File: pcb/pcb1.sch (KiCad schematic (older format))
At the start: 11 parts, among them J1 Screw_Terminal_01x02, J2 Screw_Terminal_01x02, K1 JQC-3F-_T73_-1Z-12VDC, K2 JQC-3F-_T73_-1Z-12VDC, Q1 BC547, Q2 BC547

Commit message: On attiny85 with UART Serial Support - New firmware included
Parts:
- removed A1: Arduino_Nano_v3.x, Module:Arduino_Nano, symbol MCU_Module:Arduino_Nano_v3.x
- added C1, C2: 22pF, Capacitor_THT:C_Disc_D5.0mm_W2.5mm_P5.00mm, symbol Device:C_Small
- added C3: 0.1uF, Capacitor_THT:CP_Radial_D5.0mm_P2.00mm, symbol Device:CP1
- added J3: USB_A, Connector_USB:USB_A_Molex_105057_Vertical, symbol Connector:USB_A
- added J4, J5: Conn_01x08_Male, Connector_PinHeader_2.54mm:PinHeader_1x08_P2.54mm_Horizontal, symbol Connector:Conn_01x08_Male
- added U1: ATtiny85-20PU, Package_DIP:DIP-8_W7.62mm, symbol MCU_Microchip_ATtiny:ATtiny85-20PU
- added Y1: Crystal, Crystal:Crystal_HC49-4H_Vertical, symbol Device:Crystal
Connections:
- wire segments 44 -> 95
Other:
- moved on the sheet: D1, D2, J1, J2, K1, K2, Q1, Q2, R1, R2

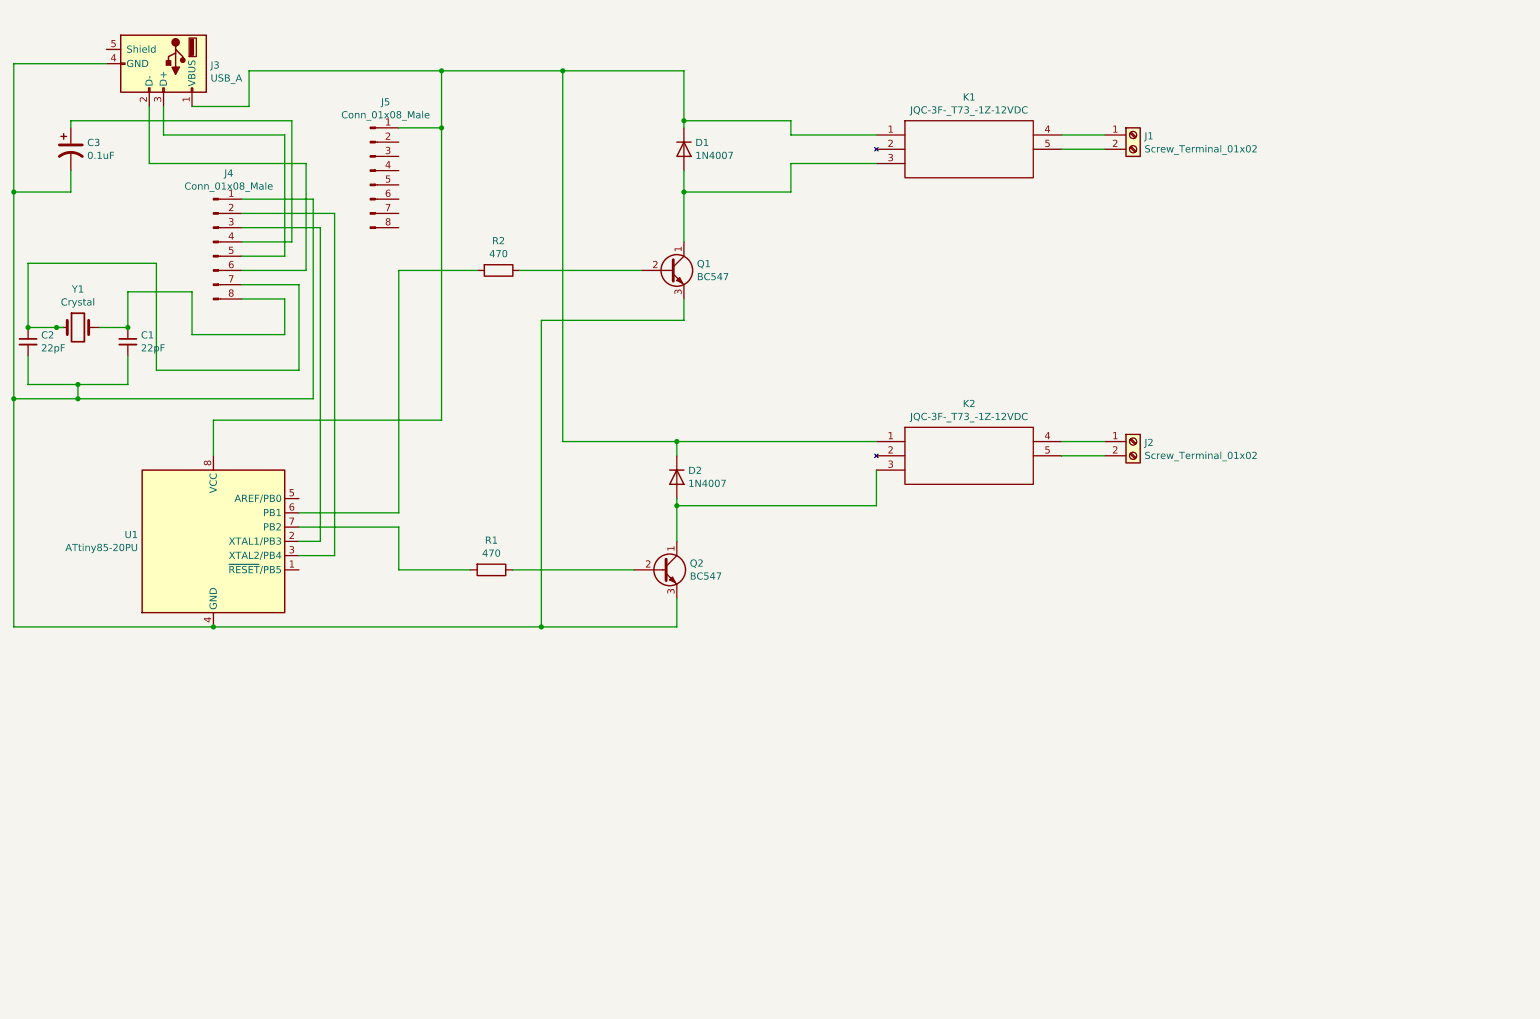
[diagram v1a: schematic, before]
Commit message: attiny85, 4 relay edition - Added MUX for greater pin support
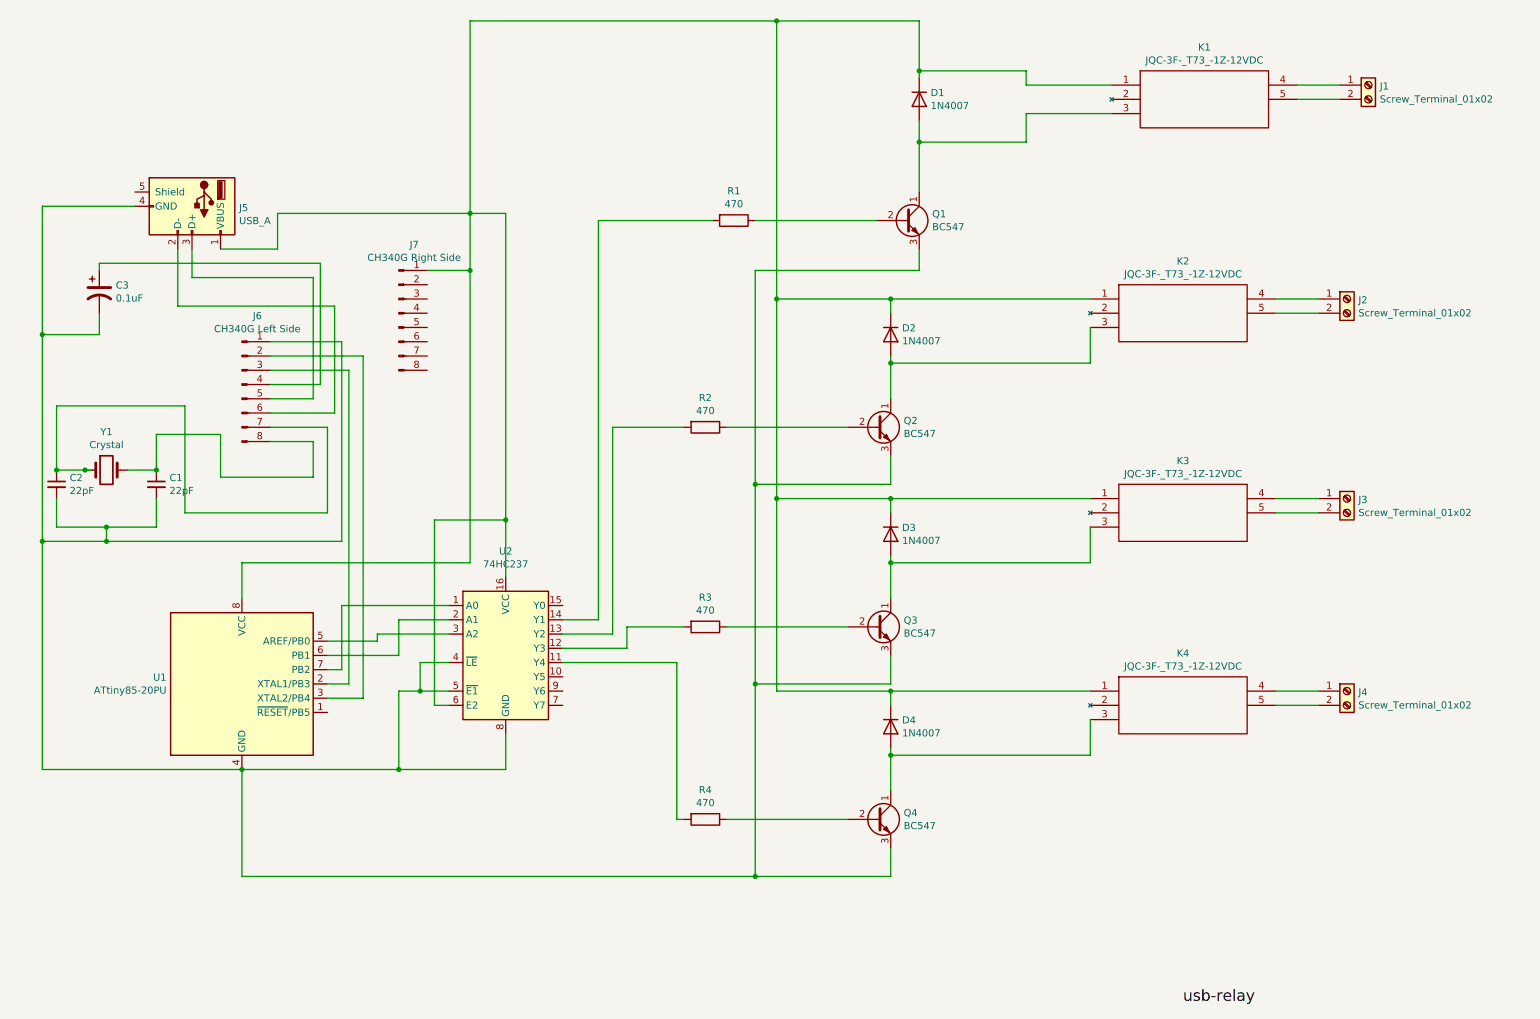
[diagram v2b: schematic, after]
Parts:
- added D3, D4: 1N4007, Diode_THT:D_DO-41_SOD81_P10.16mm_Horizontal, symbol Diode:1N4007
- added J3, J4: Screw_Terminal_01x02, TerminalBlock:TerminalBlock_Altech_AK300-2_P5.00mm, symbol Connector:Screw_Terminal_01x02
- added K3, K4: JQC-3F-_T73_-1Z-12VDC, JQC-3F-_T73_-1Z-12VDC:JQC3FT731Z12VDC, symbol JQC-3F-_T73_-1Z-12VDC:JQC-3F-_T73_-1Z-12VDC
- added Q3, Q4: BC547, Package_TO_SOT_THT:TO-92_Inline, symbol Transistor_BJT:BC547
- added R3, R4: 470, Resistor_THT:R_Axial_DIN0411_L9.9mm_D3.6mm_P12.70mm_Horizontal, symbol Device:R
- added U2: 74HC237, Package_DIP:DIP-16_W7.62mm, symbol 74xx:74HC237
- J6: renamed from J4; value Conn_01x08_Male -> CH340G Left Side
- J7: renamed from J5; value Conn_01x08_Male -> CH340G Right Side
- renumbered J3 to J5, R2 to R1, R1 to R2
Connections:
- net at C1.2, C2.2, C3.2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: now also Q3.3 (E), Q4.3 (E), U2.4 (~LE), U2.5 (~E1), U2.8 (GND)
- net at D1.1 (K), D2.1 (K), J5.1 (VBUS)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: now also D3.1 (K), D4.1 (K), K3.1, K4.1, U2.16 (VCC), U2.6 (E2)
- net at R2.2: now also U2.13 (Y2); no longer U1.7 (PB2)
- net at R1.2: now also U2.14 (Y1); no longer U1.6 (PB1)
- net at U1.5 (AREF/PB0): now also U2.3 (A2)
- new net: U1.6 (PB1), U2.2 (A1)
- new net: U1.7 (PB2), U2.1 (A0)
- new net: R4.2, U2.11 (Y4)
- new net: R3.2, U2.12 (Y3)
- new net: D3.2 (A), K3.3, Q3.1 (C)
- new net: Q3.2 (B), R3.1
- new net: J3.1 (Pin_1), K3.4
- new net: J3.2 (Pin_2), K3.5
- new net: D4.2 (A), K4.3, Q4.1 (C)
- new net: Q4.2 (B), R4.1
- new net: J4.1 (Pin_1), K4.4
- new net: J4.2 (Pin_2), K4.5
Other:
- moved on the sheet: C1, C2, C3, D1, D2, J1, J2, J5, J6, J7, K1, K2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

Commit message: atmega328p - THT version
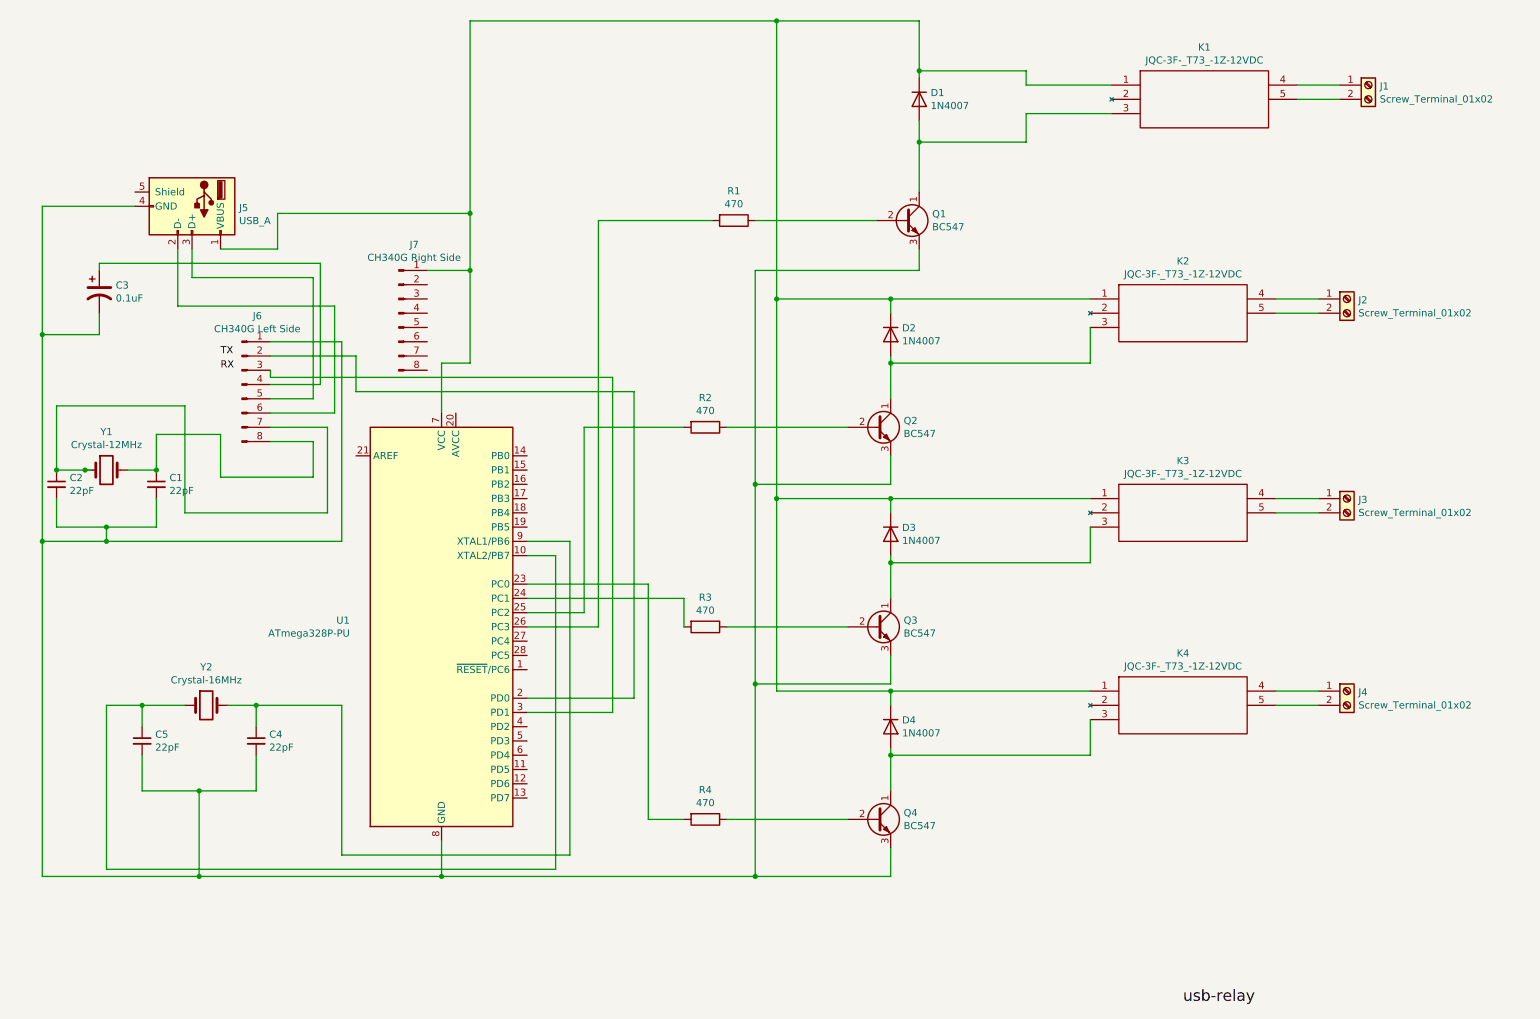
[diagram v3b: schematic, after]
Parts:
- removed U1: ATtiny85-20PU, Package_DIP:DIP-8_W7.62mm, symbol MCU_Microchip_ATtiny:ATtiny85-20PU
- removed U2: 74HC237, Package_DIP:DIP-16_W7.62mm, symbol 74xx:74HC237
- added C4, C5: 22pF, Capacitor_THT:C_Disc_D5.0mm_W2.5mm_P5.00mm, symbol Device:C_Small
- added U1: ATmega328P-PU, Package_DIP:DIP-28_W7.62mm, symbol MCU_Microchip_ATmega:ATmega328P-PU
- added Y2: Crystal-16MHz, Crystal:Crystal_HC49-4H_Vertical, symbol Device:Crystal
- Y1: value Crystal -> Crystal-12MHz
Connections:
- net at C1.2, C2.2, C3.2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: now also C4.2, C5.2, U1.22 (GND), U1.8 (GND)
- net at D1.1 (K), D2.1 (K), D3.1 (K)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: now also U1.7 (VCC)
- net at R2.2: now also U1.25 (PC2)
- net at R1.2: now also U1.26 (PC3)
- net at J6.3 (Pin_3): now also U1.3 (PD1)
- net at J6.2 (Pin_2): now also U1.2 (PD0)
- net at R4.2: now also U1.23 (PC0)
- net at R3.2: now also U1.24 (PC1)
- new net: C5.1, U1.10 (XTAL2/PB7), Y2.1
- new net: C4.1, U1.9 (XTAL1/PB6), Y2.2
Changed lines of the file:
@@
 $EndDescr
-$Comp
-L MCU_Microchip_ATtiny:ATtiny85-20PU U1
-U 1 1 6058B098
-P 2150 5250
-F 0 "U1" H 1621 5296 50  0000 R CNN
-F 1 "ATtiny85-20PU" H 1621 5205 50  0000 R CNN
-F 2 "Package_DIP:DIP-8_W7.62mm" H 2150 5250 50  0001 C CIN
-F 3 "http://ww1.microchip.com/downloads/en/DeviceDoc/atmel-2586-avr-8-bit-microcontroller-attiny25-attiny45-attiny85_datasheet.pdf" H 2150 5250 50  0001 C CNN
-	1    2150 5250
-	1    0    0    -1
-$EndComp
 $Comp
 L Transistor_BJT:BC547 Q2
@@
 P 1200 3750
 F 0 "Y1" H 1200 4018 50  0000 C CNN
-F 1 "Crystal" H 1200 3927 50  0000 C CNN
+F 1 "Crystal-12MHz" H 1200 3927 50  0000 C CNN
 F 2 "Crystal:Crystal_HC49-4H_Vertical" H 1200 3750 50  0001 C CNN
 F 3 "~" H 1200 3750 50  0001 C CNN
@@
 	1200 4150 850  4150
 Wire Wire Line
-	1400 1900 750  1900
-Wire Wire Line
 	750  1900 750  2800
 Wire Wire Line
@@
 Wire Wire Line
 	1050 3750 850  3750
-Wire Wire Line
-	2150 5850 750  5850
-Wire Wire Line
-	750  5850 750  4250
 Connection ~ 750  4250
 $Comp
@@
 	2000 2200 2400 2200
 Wire Wire Line
-	2150 4650 2150 4400
-Wire Wire Line
 	2400 1950 2400 2200
 Wire Wire Line
@@
 Wire Wire Line
 	6900 2200 6900 2350
-Wire Wire Line
-	2900 5250 2750 5250
-Wire Wire Line
-	2750 5350 3000 5350
 $Comp
 L Connector:Conn_01x08_Male J6
@@
 $EndComp
 Wire Wire Line
-	2150 4400 3750 4400
-Wire Wire Line
-	3750 4400 3750 2350
-Wire Wire Line
 	3750 2350 3450 2350
 Wire Wire Line
 	3750 1950 3750 2350
-Wire Wire Line
-	3750 1950 2400 1950
-Connection ~ 3750 2350
 Wire Wire Line
 	1750 3300 850  3300
@@
 	2350 3150 2700 3150
 Wire Wire Line
-	2900 3050 2350 3050
-Wire Wire Line
-	2900 5250 2900 3050
-Wire Wire Line
-	3000 2950 3000 5350
-Wire Wire Line
-	2350 2950 3000 2950
-Wire Wire Line
-	2850 2850 2850 4250
-Wire Wire Line
 	2350 2850 2850 2850
-$Comp
-L 74xx:74HC237 U2
-U 1 1 605E4E2C
-P 4000 5100
-F 0 "U2" H 4000 5881 50  0000 C CNN
-F 1 "74HC237" H 4000 5790 50  0000 C CNN
-F 2 "Package_DIP:DIP-16_W7.62mm" H 4000 5100 50  0001 C CNN
-F 3 "http://www.ti.com/lit/ds/symlink/cd74hc237.pdf" H 4000 5100 50  0001 C CNN
-	1    4000 5100
-	1    0    0    -1
-$EndComp
-Wire Wire Line
-	2750 5050 3250 5050
-Wire Wire Line
-	3250 5050 3250 4800
-Wire Wire Line
-	3250 4800 3600 4800
 Wire Wire Line
 	5750 3850 5750 2350
@@
 Wire Wire Line
 	6700 5250 5750 5250
-Wire Wire Line
-	5450 2000 4650 2000
-Wire Wire Line
-	4650 2000 4650 4800
-Wire Wire Line
-	4650 4800 4400 4800
-Wire Wire Line
-	4400 4900 4750 4900
-Wire Wire Line
-	4750 4900 4750 3450
-Wire Wire Line
-	4750 3450 5250 3450
-Wire Wire Line
-	5250 4850 4850 4850
-Wire Wire Line
-	4850 4850 4850 5000
-Wire Wire Line
-	4850 5000 4400 5000
 $Comp
 L Transistor_BJT:BC547 Q4
@@
 Connection ~ 6700 5300
 Wire Wire Line
-	4400 5100 5200 5100
-Wire Wire Line
-	5200 5100 5200 6200
-Wire Wire Line
-	5200 6200 5250 6200
-Wire Wire Line
 	6700 6600 5750 6600
-Wire Wire Line
-	2150 6600 2150 5850
-Connection ~ 2150 5850
-Wire Wire Line
-	4000 5600 4000 5850
-Wire Wire Line
-	4000 5850 3250 5850
-Wire Wire Line
-	3600 5300 3400 5300
-Wire Wire Line
-	3250 5300 3250 5850
-Connection ~ 3250 5850
-Wire Wire Line
-	3250 5850 2150 5850
-Wire Wire Line
-	4000 4500 4000 4100
-Wire Wire Line
-	4000 1950 3750 1950
-Wire Wire Line
-	3600 5400 3500 5400
-Wire Wire Line
-	3500 5400 3500 4100
-Wire Wire Line
-	3500 4100 4000 4100
-Connection ~ 4000 4100
-Wire Wire Line
-	4000 4100 4000 1950
-Wire Wire Line
-	3600 5100 3400 5100
-Wire Wire Line
-	3400 5100 3400 5300
-Connection ~ 3400 5300
-Wire Wire Line
-	3400 5300 3250 5300
 Text Label 8750 7500 0    79   ~ 0
 usb-relay
-Wire Wire Line
-	3600 4900 3100 4900
-Wire Wire Line
-	3100 4900 3100 4950
-Wire Wire Line
-	3100 4950 2750 4950
-Wire Wire Line
-	3600 4700 2850 4700
-Wire Wire Line
-	2850 4700 2850 5150
-Wire Wire Line
-	2850 5150 2750 5150
 Wire Wire Line
 	5550 6200 6400 6200
@@
 Connection ~ 5750 6600
 Wire Wire Line
-	5750 6600 2150 6600
+	750  4250 750  6600
+Wire Wire Line
+	750  6600 1850 6600
+Wire Wire Line
+	4900 5350 4900 3200
+Wire Wire Line
+	4900 3200 2950 3200
+Wire Wire Line
+	2950 3200 2950 2950
+Wire Wire Line
+	2950 2950 2350 2950
+Wire Wire Line
+	4750 3100 2350 3100
+Wire Wire Line
+	2350 3100 2350 3050
+Text Label 2000 2950 0    50   ~ 0
+TX
+Text Label 2000 3050 0    50   ~ 0
+RX
+$Comp
+L Device:Crystal Y2
+U 1 1 6069FCFD
+P 1900 5400
+F 0 "Y2" H 1900 5668 50  0000 C CNN
+F 1 "Crystal-16MHz" H 1900 5577 50  0000 C CNN
+F 2 "Crystal:Crystal_HC49-4H_Vertical" H 1900 5400 50  0001 C CNN
+F 3 "~" H 1900 5400 50  0001 C CNN
+	1    1900 5400
+	1    0    0    -1
+$EndComp
+$Comp
+L Device:C_Small C5
+U 1 1 606A3350
+P 1450 5650
+F 0 "C5" H 1542 5696 50  0000 L CNN
+F 1 "22pF" H 1542 5605 50  0000 L CNN
+F 2 "Capacitor_THT:C_Disc_D5.0mm_W2.5mm_P5.00mm" H 1450 5650 50  0001 C CNN
+F 3 "~" H 1450 5650 50  0001 C CNN
+	1    1450 5650
+	1    0    0    -1
+$EndComp
+$Comp
+L Device:C_Small C4
+U 1 1 606A8D1A
+P 2250 5650
+F 0 "C4" H 2342 5696 50  0000 L CNN
+F 1 "22pF" H 2342 5605 50  0000 L CNN
+F 2 "Capacitor_THT:C_Disc_D5.0mm_W2.5mm_P5.00mm" H 2250 5650 50  0001 C CNN
+F 3 "~" H 2250 5650 50  0001 C CNN
+	1    2250 5650
+	1    0    0    -1
+$EndComp
+Wire Wire Line
+	2250 5750 2250 6000
+Wire Wire Line
+	2250 6000 1850 6000
+Wire Wire Line
+	1450 6000 1450 5750
+Wire Wire Line
+	1850 6000 1850 6600
+Connection ~ 1850 6000
+Wire Wire Line
+	1850 6000 1450 6000
+Connection ~ 1850 6600
+Wire Wire Line
+	1850 6600 3550 6600
+Wire Wire Line
+	2050 5400 2250 5400
+Wire Wire Line
+	2250 5400 2250 5550
+Wire Wire Line
+	1750 5400 1450 5400
+Wire Wire Line
+	1450 5400 1450 5550
+Wire Wire Line
+	4750 5450 4750 3100
+Wire Wire Line
+	2850 2850 2850 4250
+$Comp
+L MCU_Microchip_ATmega:ATmega328P-PU U1
+U 1 1 6065D461
+P 3550 4850
+F 0 "U1" H 2906 4896 50  0000 R CNN
+F 1 "ATmega328P-PU" H 2906 4805 50  0000 R CNN
+F 2 "Package_DIP:DIP-28_W7.62mm" H 3550 4850 50  0001 C CIN
+F 3 "http://ww1.microchip.com/downloads/en/DeviceDoc/ATmega328_P%20AVR%20MCU%20with%20picoPower%20Technology%20Data%20Sheet%2040001984A.pdf" H 3550 4850 50  0001 C CNN
+	1    3550 4850
+	1    0    0    -1
+$EndComp
+Wire Wire Line
+	4150 5350 4900 5350
+Wire Wire Line
+	4150 5450 4750 5450
+Wire Wire Line
+	3550 6350 3550 6600
+Connection ~ 3550 6600
+Wire Wire Line
+	3550 3350 3550 3000
+Wire Wire Line
+	3550 3000 3750 3000
+Wire Wire Line
+	3750 3000 3750 2350
+Connection ~ 3750 2350
+Wire Wire Line
+	3550 6600 5750 6600
+Wire Wire Line
+	4150 4250 4450 4250
+Wire Wire Line
+	2850 5400 2250 5400
+Connection ~ 2250 5400
+Wire Wire Line
+	4150 4350 4350 4350
+Wire Wire Line
+	1200 5400 1450 5400
+Connection ~ 1450 5400
+Wire Wire Line
+	5450 2000 4650 2000
+Wire Wire Line
+	4650 2000 4650 4850
+Wire Wire Line
+	4650 4850 4150 4850
+Wire Wire Line
+	4550 3450 4550 4750
+Wire Wire Line
+	4550 4750 4150 4750
+Wire Wire Line
+	4550 3450 5250 3450
+Wire Wire Line
+	4150 4650 5250 4650
+Wire Wire Line
+	5250 4650 5250 4850
+Wire Wire Line
+	4150 4550 5000 4550
+Wire Wire Line
+	5000 4550 5000 6200
+Wire Wire Line
+	5000 6200 5250 6200
+Wire Wire Line
+	4350 6550 1200 6550
+Wire Wire Line
+	4350 4350 4350 6550
+Wire Wire Line
+	1200 5400 1200 6550
+Wire Wire Line
+	2850 5400 2850 6450
+Wire Wire Line
+	2850 6450 4450 6450
+Wire Wire Line
+	4450 4250 4450 6450
+Wire Wire Line
+	2400 1950 3750 1950
+Wire Wire Line
+	750  1900 1400 1900
 $EndSCHEMATC

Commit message: Finalized attiny85 design
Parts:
- removed C4, C5: 22pF, Capacitor_THT:C_Disc_D5.0mm_W2.5mm_P5.00mm, symbol Device:C_Small
- removed D3, D4: 1N4007, Diode_THT:D_DO-41_SOD81_P10.16mm_Horizontal, symbol Diode:1N4007
- removed J3, J4: Screw_Terminal_01x02, TerminalBlock:TerminalBlock_Altech_AK300-2_P5.00mm, symbol Connector:Screw_Terminal_01x02
- removed K3, K4: JQC-3F-_T73_-1Z-12VDC, JQC-3F-_T73_-1Z-12VDC:JQC3FT731Z12VDC, symbol JQC-3F-_T73_-1Z-12VDC:JQC-3F-_T73_-1Z-12VDC
- removed Q3, Q4: BC547, Package_TO_SOT_THT:TO-92_Inline, symbol Transistor_BJT:BC547
- removed R3, R4: 470, Resistor_THT:R_Axial_DIN0411_L9.9mm_D3.6mm_P12.70mm_Horizontal, symbol Device:R
- removed U1: ATmega328P-PU, Package_DIP:DIP-28_W7.62mm, symbol MCU_Microchip_ATmega:ATmega328P-PU
- removed Y2: Crystal-16MHz, Crystal:Crystal_HC49-4H_Vertical, symbol Device:Crystal
- added U1: ATtiny85-20PU, Package_DIP:DIP-8_W7.62mm, symbol MCU_Microchip_ATtiny:ATtiny85-20PU
- J4: renamed from J6; value CH340G Left Side -> CH340G - LEFT
- J5: renamed from J7; value CH340G Right Side -> CH340G - RIGHT
- Y1: value Crystal-12MHz -> Crystal
- renumbered J5 to J3, R2 to R1, R1 to R2
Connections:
- net at D1.2 (A), Q1.1 (C): now also K1.1; no longer K1.3
- net at C1.2, C2.2, C3.2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: now also U1.4 (GND)
- net at D2.2 (A), Q2.1 (C): now also K2.1; no longer K2.3
- net at D1.1 (K), D2.1 (K), J3.1 (VBUS)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: now also K1.4, K2.4, U1.8 (VCC); no longer K1.1, K2.1
- net at R1.2: now also U1.7 (PB2)
- net at R2.2: now also U1.6 (PB1)
- net at J1.1 (Pin_1): now also K1.5; no longer K1.4
- net at J1.2 (Pin_2): now also K1.3; no longer K1.5
- net at J2.1 (Pin_1): now also K2.5; no longer K2.4
- net at J2.2 (Pin_2): now also K2.3; no longer K2.5
- net at J4.2 (Pin_2): now also U1.3 (XTAL2/PB4)
- net at J4.3 (Pin_3): now also U1.2 (XTAL1/PB3)
- net XO: now reaches C1.1, J4.8 (Pin_8), Y1.2
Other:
- moved on the sheet: C1, C2, C3, D1, D2, J1, J2, J3, J4, J5, K1, K2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
